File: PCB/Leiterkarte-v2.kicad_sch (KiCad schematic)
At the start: 46 parts

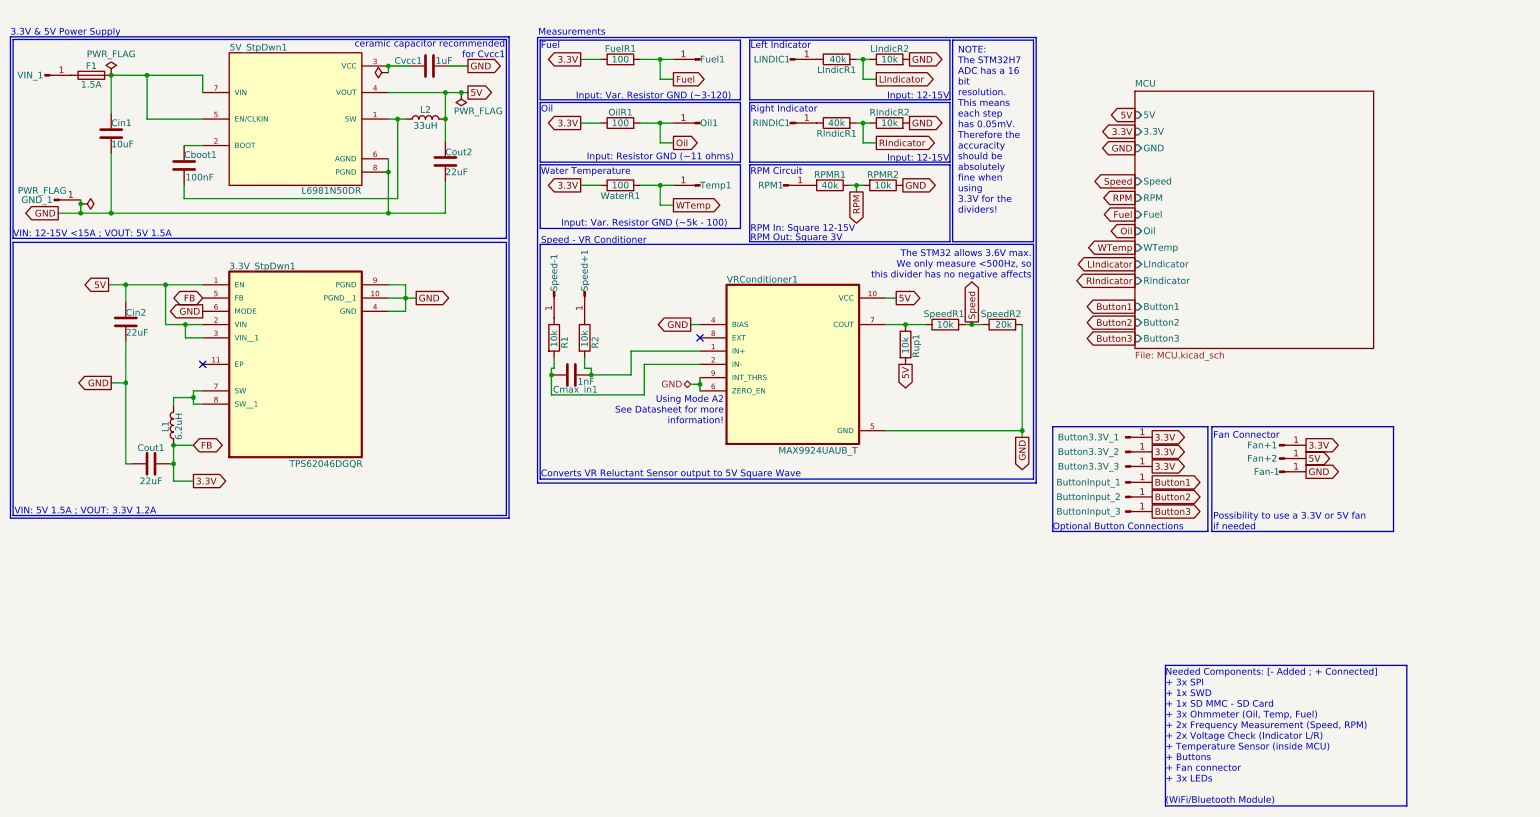
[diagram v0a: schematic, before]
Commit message: Updated component selection; Updated some footprints; Added .csv file in the export folder of the PCB that contains parts from DigiKey
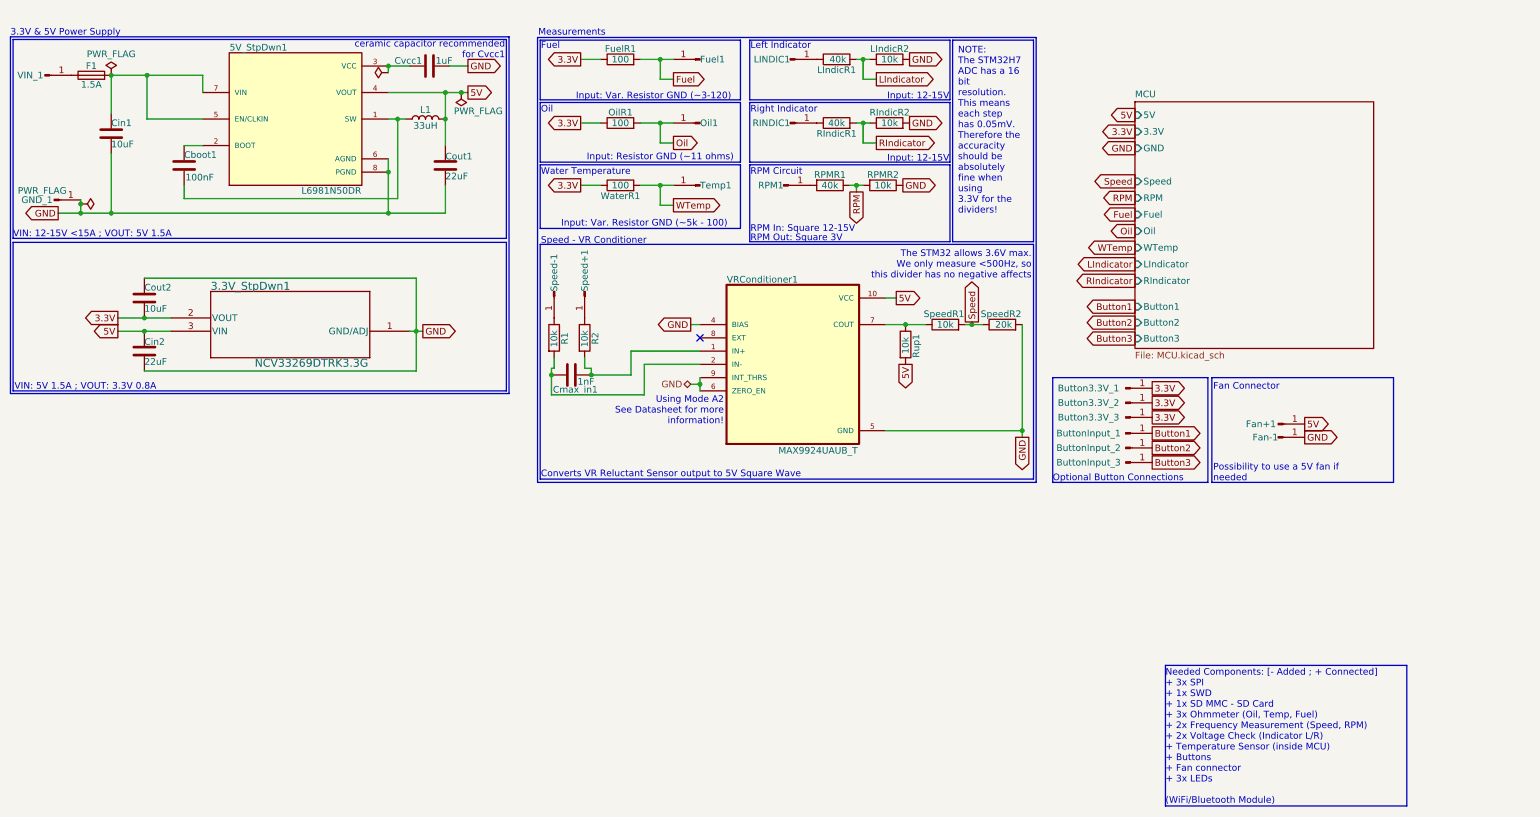
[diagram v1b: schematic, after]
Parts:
- removed 3.3V_StpDwn1: TPS62046DGQR, TPS62046DGQR:IC_XTR111AIDGQR, symbol TPS62046DGQR:TPS62046DGQR
- removed Fan+1: Conn_01x01_Pin, Connector_PinHeader_2.54mm:PinHeader_1x01_P2.54mm_Vertical, symbol Connector:Conn_01x01_Pin
- removed L1: 6.2uH, Inductor_SMD:L_6.3x6.3_H3, symbol Device:L
- added 3.3V_StpDwn1: NCV33269DTRK3.3G, NCV33269DTRK3.3G:DPAK-3_ONS-M, symbol NCV33269DTRK3.3G:NCV33269DTRK3.3G
- Cboot1, Cmax_in1, Cvcc1: footprint Capacitor_SMD:C_0603_1608Metric -> Capacitor_SMD:C_0805_2012Metric
- Cout2: value 22uF -> 10uF
- renumbered Fan+2 to Fan+1, L2 to L1
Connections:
- net 3.3V: now also Cout2.2, 3.3V_StpDwn1.2 (VOUT); no longer Cout1.2
- net 5V: now also Cout1.1, 3.3V_StpDwn1.3 (VIN); no longer Cout2.1
- net GND: now also Cout1.2, Cout2.1, 3.3V_StpDwn1.1 (GND/ADJ); no longer Cout1.1, Cout2.2
- no-connect marks 2 -> 1
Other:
- note added: "Possibility to use a 5V fan if needed"
- note added: "VIN: 5V 1.5A ; VOUT: 3.3V 0.8A"
- note removed: "Possibility to use a 3.3V or 5V fan if needed"
- note removed: "VIN: 5V 1.5A ; VOUT: 3.3V 1.2A"
- moved on the sheet: Button3.3V_1, Button3.3V_2, Button3.3V_3, ButtonInput_1, ButtonInput_2, ButtonInput_3, Cin2, Fan+1, Fan-1

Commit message: Added 2x Temperature Sensors; Updated wrong GPIO connections in schematic; Set Button input GPIOs to Pull-Down; LED circuits need to be corrected
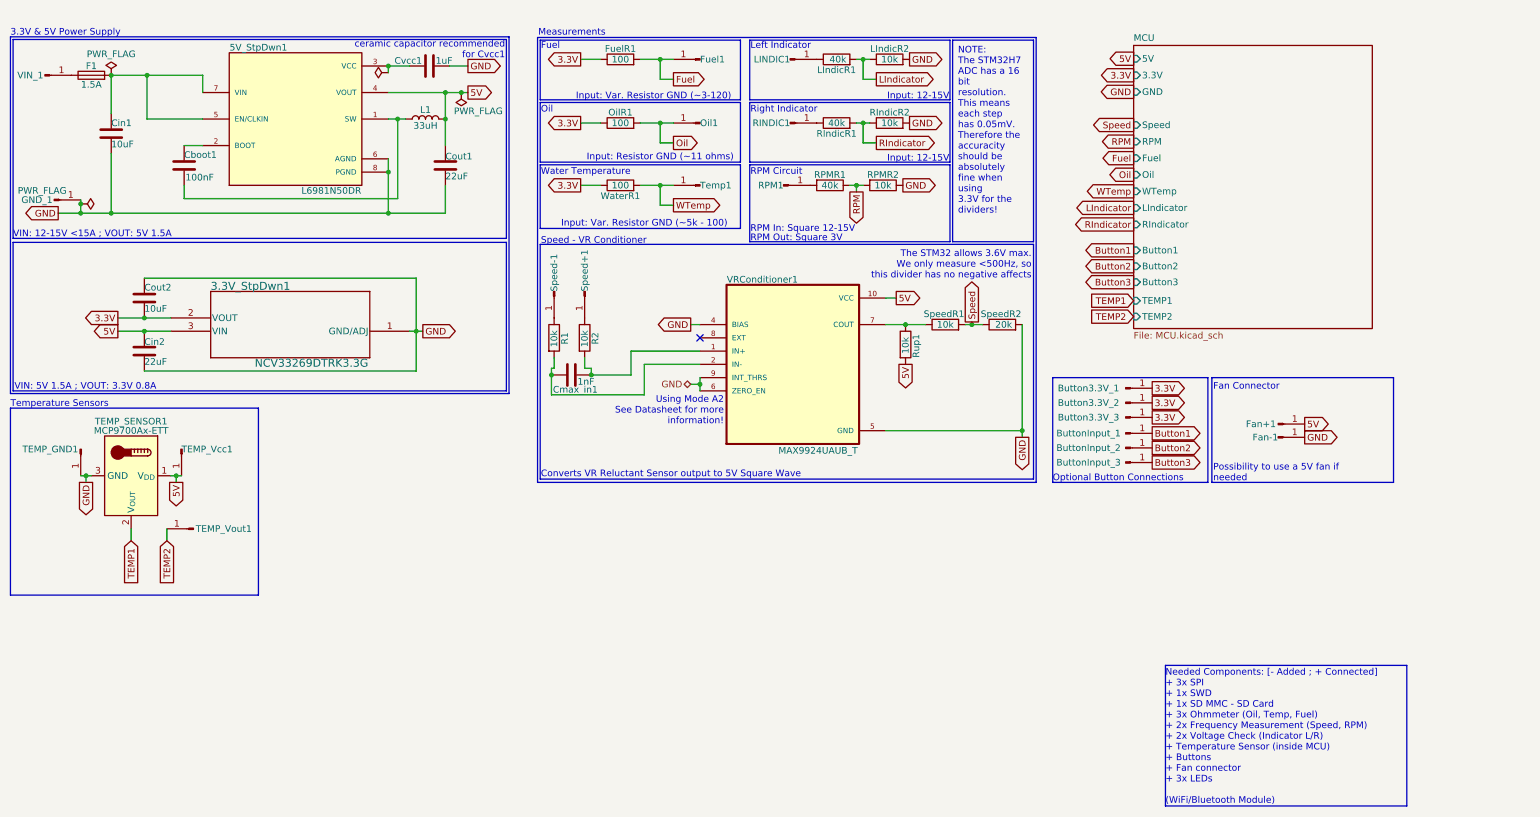
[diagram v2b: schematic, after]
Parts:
- added TEMP_GND1, TEMP_Vcc1, TEMP_Vout1: Conn_01x01_Pin, symbol Connector:Conn_01x01_Pin
- added TEMP_SENSOR1: MCP9700Ax-ETT, Package_TO_SOT_SMD:SOT-23, symbol Sensor_Temperature:MCP9700Ax-ETT
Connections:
- net 5V: now also TEMP_SENSOR1.1 (V_{DD}), TEMP_Vcc1.1 (Pin_1)
- net GND: now also TEMP_GND1.1 (Pin_1), TEMP_SENSOR1.3 (GND)
- new net TEMP1: TEMP_SENSOR1.2 (V_{OUT})
- new net TEMP2: TEMP_Vout1.1 (Pin_1)
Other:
- sheet MCU ports: added TEMP1, TEMP2; removed none
- note added: "Temperature Sensors"

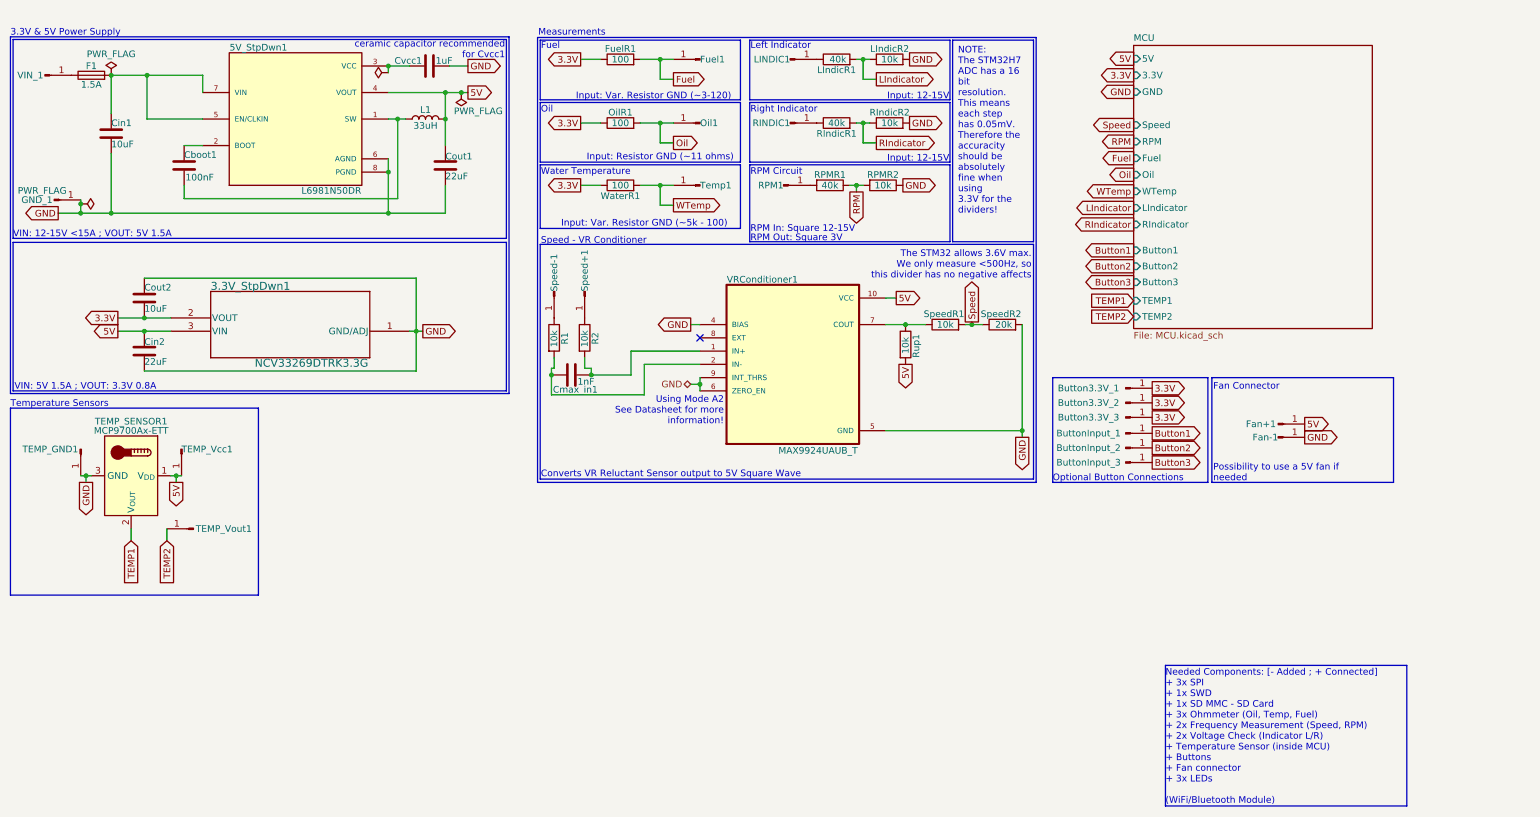
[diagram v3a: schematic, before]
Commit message: Switched from L6981N50DR to TPS5430DDAR
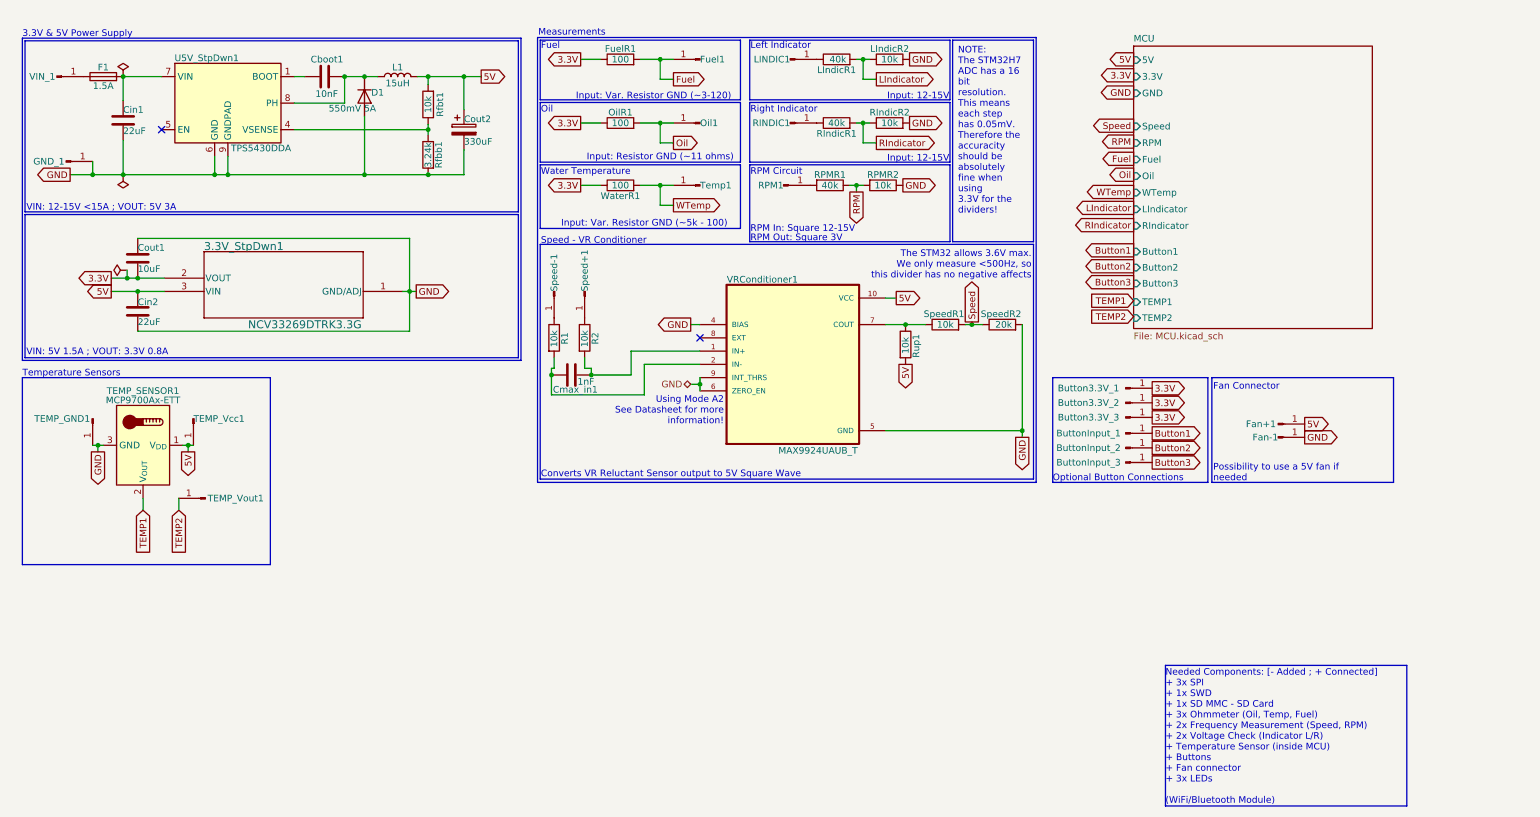
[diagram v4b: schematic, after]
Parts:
- removed 5V_StpDwn1: L6981N50DR, L6981N50DR:SOIC127P600X175-8N, symbol L6981N50DR:L6981N50DR
- removed Cout2: 10uF, Capacitor_SMD:C_0805_2012Metric, symbol Device:C
- removed Cvcc1: 1uF, Capacitor_SMD:C_0805_2012Metric, symbol Device:C
- added Cout2: 330uF, symbol Device:C_Polarized
- added D1: 550mV 5A, symbol Device:D
- added Rfbb1: 3.24k, symbol Device:R
- added Rfbt1: 10k, symbol Device:R
- added U5V_StpDwn1: TPS5430DDA, Package_SO:TI_SO-PowerPAD-8_ThermalVias, symbol Regulator_Switching:TPS5430DDA
- Cboot1: value 100nF -> 10nF
- Cin1: value 10uF -> 22uF
- Cout1: value 22uF -> 10uF
- L1: value 33uH -> 15uH
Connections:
- net 3.3V: now also Cout1.2
- net 5V: now also Cout2.1, Rfbt1.2; no longer Cout1.1
- net GND: now also Cout1.1, Cout2.2, D1.2 (A), Rfbb1.2, U5V_StpDwn1.6 (GND), U5V_StpDwn1.9 (GNDPAD); no longer Cout1.2
- net at Cboot1.1, L1.1: now also D1.1 (K), U5V_StpDwn1.8 (PH)
- net at Cboot1.2: now also U5V_StpDwn1.1 (BOOT)
- net at Cin1.1, F1.2: now also U5V_StpDwn1.7 (VIN)
- new net: Rfbb1.1, Rfbt1.1, U5V_StpDwn1.4 (VSENSE)
- no-connect marks 1 -> 2
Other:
- note added: "VIN: 12-15V <15A ; VOUT: 5V 3A"
- note removed: "VIN: 12-15V <15A ; VOUT: 5V 1.5A"
- note removed: "ceramic capacitor recommended for Cvcc1"

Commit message: Replaced some global labels with power net(s); Added warning label for missing component
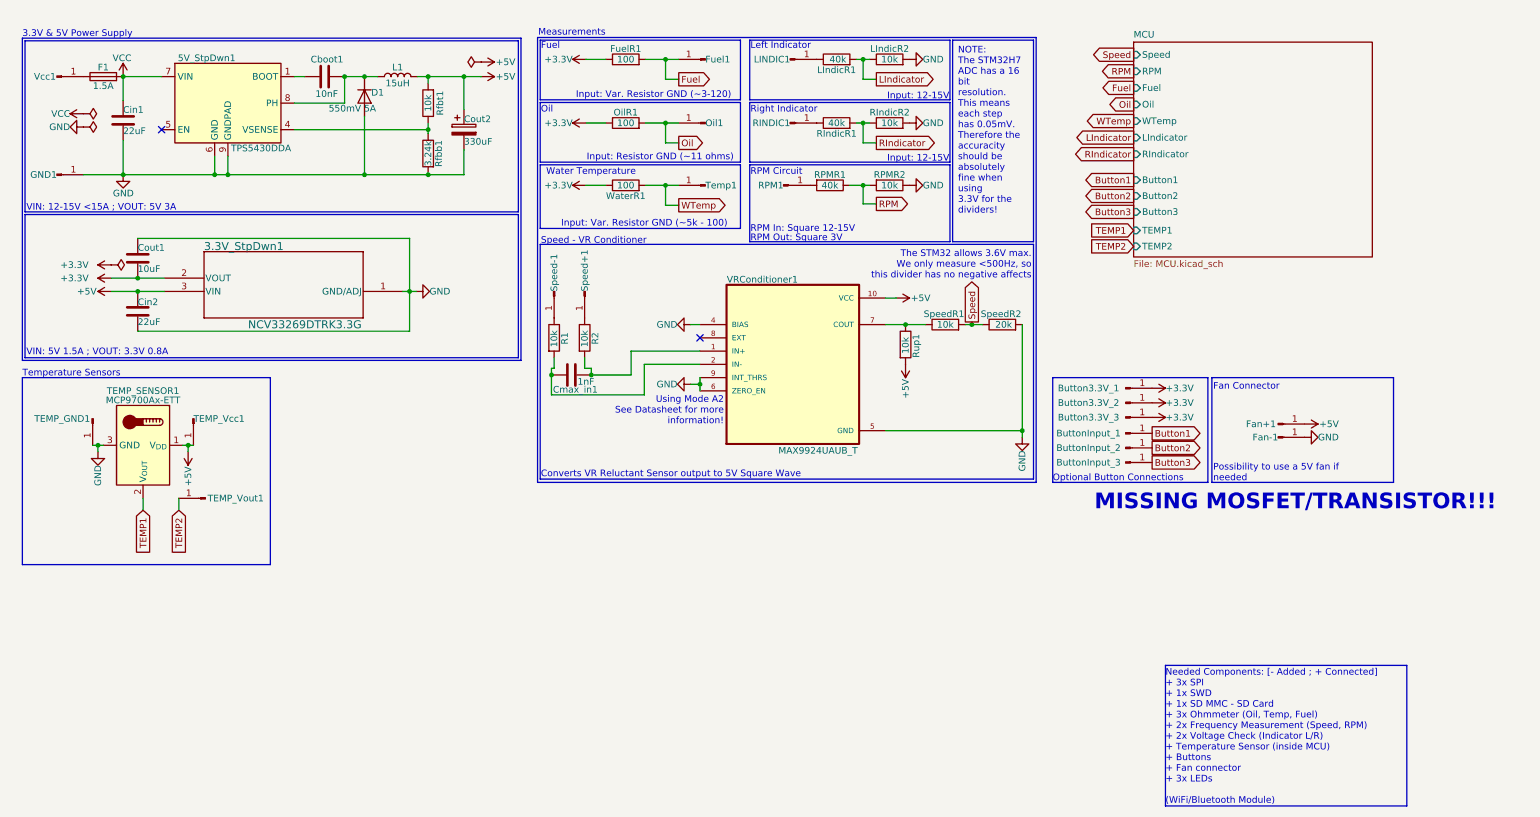
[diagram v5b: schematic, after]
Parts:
- removed GND_1, VIN_1: Conn_01x01_Pin, Connector_Wire:SolderWire-0.75sqmm_1x01_D1.25mm_OD3.5mm, symbol Connector:Conn_01x01_Pin
- added GND1, Vcc1: Conn_01x01_Pin, Connector_PinHeader_2.54mm:PinHeader_1x01_P2.54mm_Vertical, symbol Connector:Conn_01x01_Pin
- Cout2: footprint (none) -> Capacitor_SMD:C_0805_2012Metric
- D1: footprint (none) -> Diode_SMD:D_0805_2012Metric
- Rfbb1, Rfbt1: footprint (none) -> Resistor_SMD:R_0603_1608Metric
- TEMP_GND1, TEMP_Vcc1, TEMP_Vout1: footprint (none) -> Connector_PinHeader_2.54mm:PinHeader_1x01_P2.54mm_Vertical
- renumbered U5V_StpDwn1 to 5V_StpDwn1
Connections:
- net GND: now also GND1.1 (Pin_1)
- net at F1.1: now also Vcc1.1 (Pin_1)
- net VCC: now reaches 5V_StpDwn1.7 (VIN), Cin1.1, F1.2
- net 3.3V renamed +3.3V
- net 5V renamed +5V
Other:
- sheet MCU ports: added none; removed 3.3V, 5V, GND
- note added: "MISSING MOSFET/TRANSISTOR!!!"
- moved on the sheet: Fuel1, FuelR1, Oil1, RPMR2, Temp1, WaterR1
